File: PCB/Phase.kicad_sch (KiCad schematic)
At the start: 18 parts, among them J4 Mot_Con, Q1 P75NF75, Q2 P75NF75, U1 UCC27282

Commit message: Uploaded working software.
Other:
- note removed: "-3dB point = 15.9kHz"
- note removed: "Selected value = 1u (increase if necessary)"
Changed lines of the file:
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@@
   )
   (text "Must size boot capacitor to account for skipped pulses and switching times!"
-    (at 93.98 58.42 0)
+    (at 95.25 68.58 0)
     (effects (font (size 1.27 1.27)) (justify left bottom))
   )
-  (text "Selected value = 1u (increase if necessary)" (at 93.98 60.96 0)
-    (effects (font (size 1.27 1.27)) (justify left bottom))
-  )
-  (text "-3dB point = 15.9kHz" (at 93.98 66.04 0)
-    (effects (font (size 1.27 1.27)) (justify left bottom))
-  )

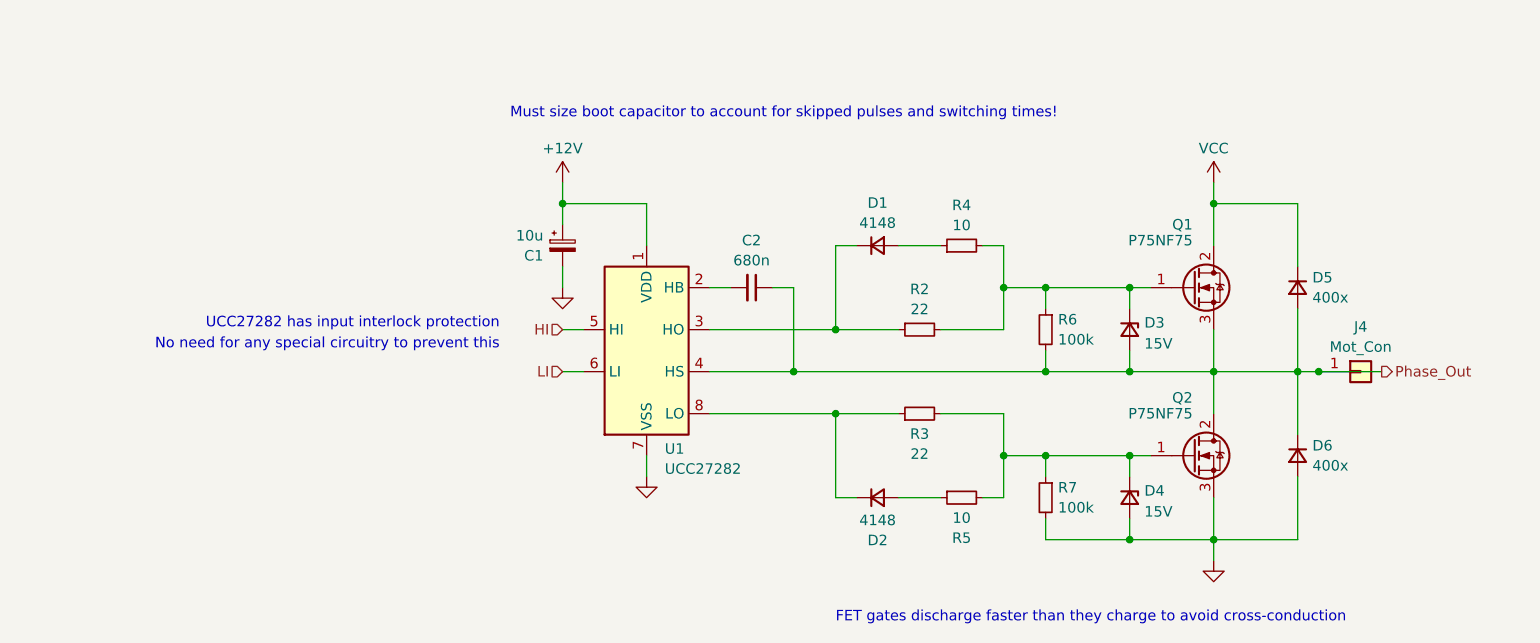
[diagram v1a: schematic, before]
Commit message: Updated to V1.1. Removed extra parts. Rearranged components. Added on-board LEDs.
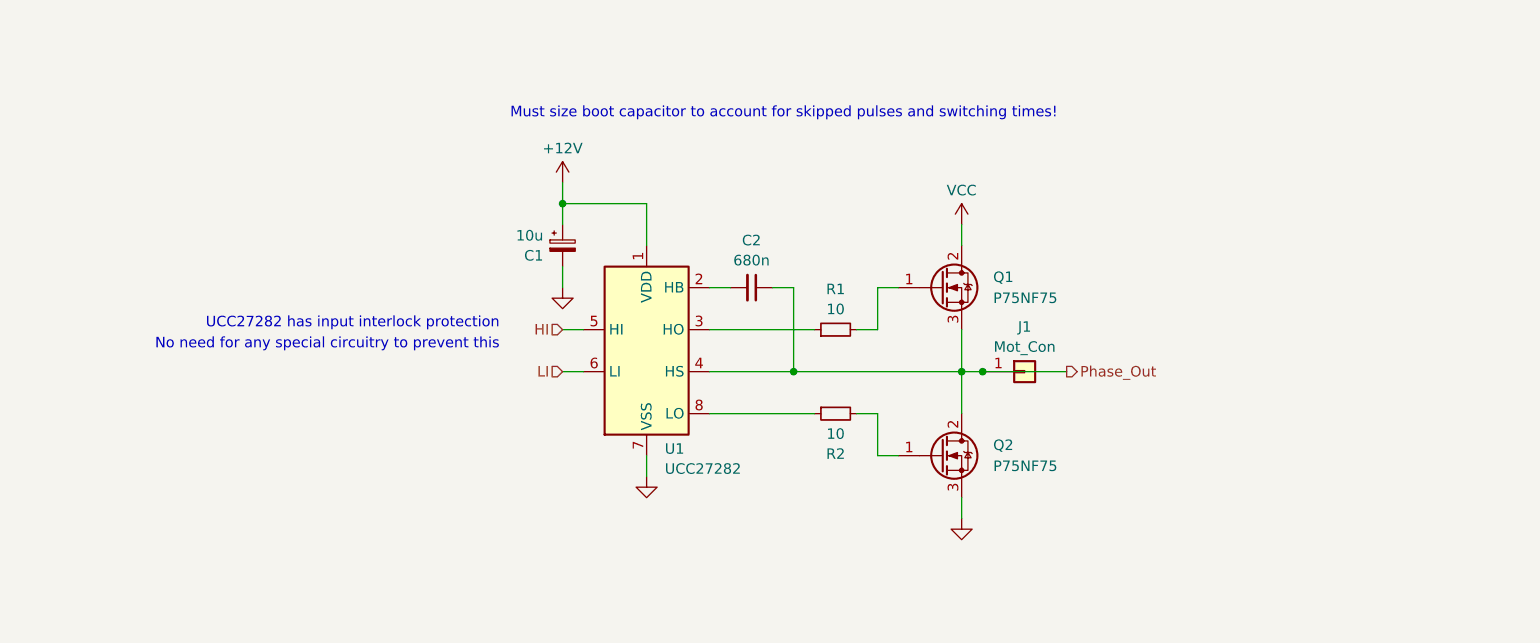
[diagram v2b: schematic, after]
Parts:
- removed D1, D2: 4148, Diode_THT:D_DO-35_SOD27_P7.62mm_Horizontal, symbol Device:D_Small
- removed D3, D4: 15V, Diode_THT:D_DO-35_SOD27_P7.62mm_Horizontal, symbol Device:D_Zener_Small
- removed D5, D6: 400x, Diode_THT:D_DO-35_SOD27_P7.62mm_Horizontal, symbol Device:D_Small
- removed R2, R3: 22, Resistor_THT:R_Axial_DIN0204_L3.6mm_D1.6mm_P7.62mm_Horizontal, symbol Device:R_Small
- removed R6, R7: 100k, Resistor_THT:R_Axial_DIN0204_L3.6mm_D1.6mm_P7.62mm_Horizontal, symbol Device:R_Small
- J1: renamed from J4; footprint Ariamelon-HolePad:MountingHole_3.2mm_M3_Pad -> TestPoint:TestPoint_Pad_4.0x4.0mm
- renumbered R4 to R1, R5 to R2
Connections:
- net at R1.1: now also U1.3 (HO)
- net at R2.1: now also U1.8 (LO)
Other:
- note removed: "FET gates discharge faster than they charge to avoid cross-conduction"
- moved on the sheet: J1, Q1, Q2, R1, R2
